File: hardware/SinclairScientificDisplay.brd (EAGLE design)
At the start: 47 x 17.8 mm, 6 parts

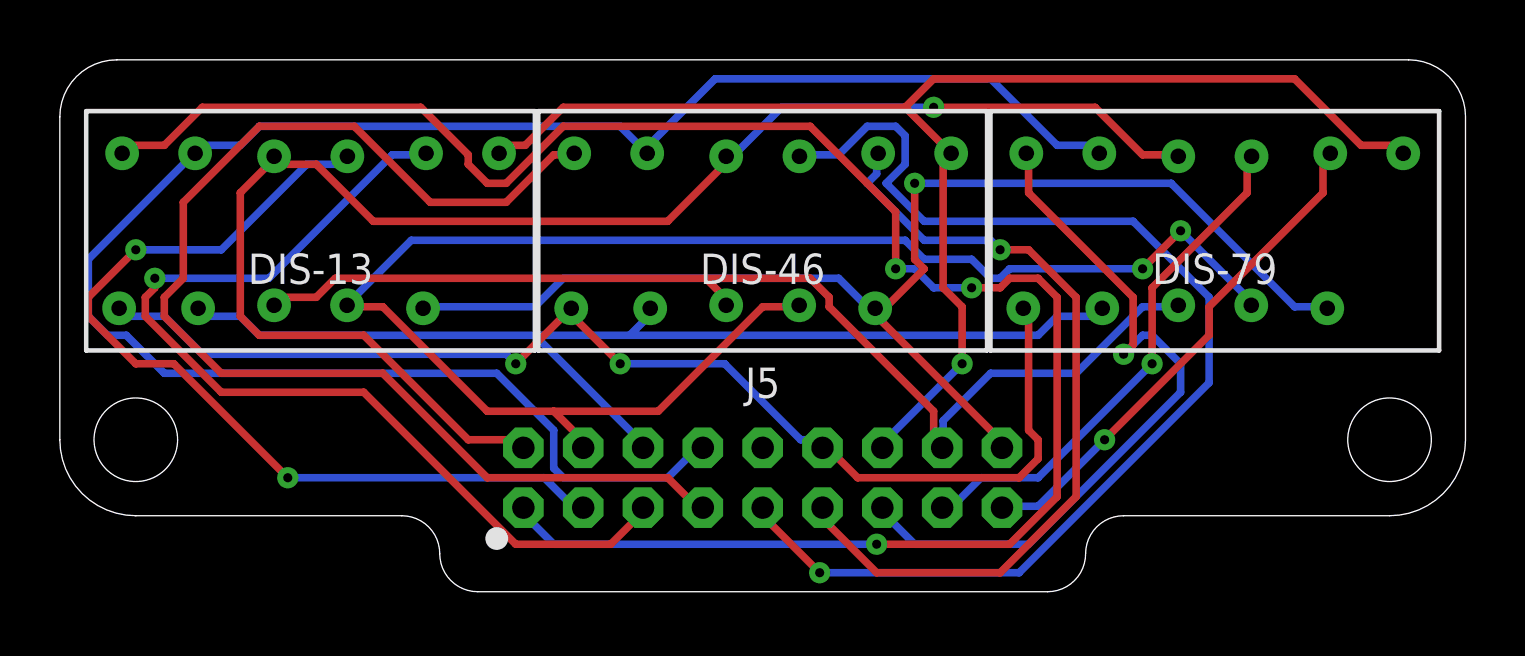
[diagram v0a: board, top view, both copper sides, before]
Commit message: Added some silkscreen labels and logo
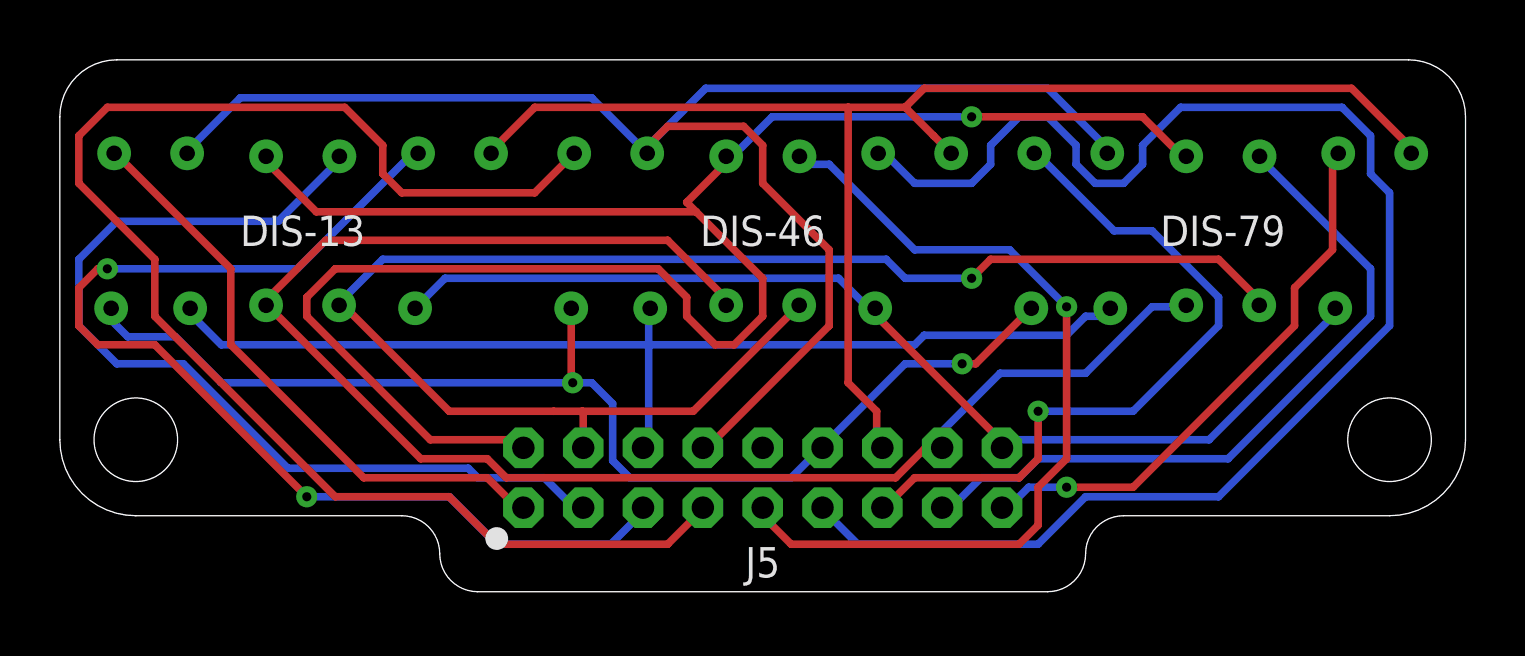
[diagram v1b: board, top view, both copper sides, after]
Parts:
- moved DIS-13 0.27 mm to (8.12, 12.1)
- moved DIS-79 0.27 mm to (38.9, 12.1)
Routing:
- net LED_CA1: track 63.5 -> 20.1 mm, vias 3 -> 0
- net LED_CA6: track 27.1 -> 50.4 mm, vias 1 -> 0
- net LED_DP: track 37.4 -> 53.4 mm
- net LED_F: track 50.6 -> 65.8 mm
- net LED_A: track 64.1 -> 51.8 mm
- net LED_CA5: track 39.8 -> 29.0 mm
- net LED_CA4: track 40.6 -> 48.3 mm
- net LED_G: track 43.3 -> 35.7 mm, vias 1 -> 0
- net LED_CA8: track 17.7 -> 24.2 mm, vias 1 -> 0
- net LED_CA3: track 32.5 -> 36.9 mm, vias 1 -> 2
- net LED_CA9: track 17.2 -> 18.7 mm
- net LED_CA2: track 30.9 -> 32.1 mm, vias 2 -> 0
- net LED_E: track 40.3 -> 39.3 mm
- net LED_D: track 37.4 -> 36.6 mm
- net LED_C: track 53.0 -> 52.2 mm, vias 2 -> 1
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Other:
- board text added: "1"
- board text added: "2"
- board text added: "3"
- board text added: "4"
- board text added: "5"
- board text added: "6"
- board text added: "7"
- board text added: "8"
- board text added: "9"
- board text added: "A"
- board text added: "B"
- board text added: "C"
- board text added: "D"
- board text added: "E"
- board text added: "F"
- board text added: "G"
- board text added: "P"

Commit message: Fixed some hardware issues found in testing v1B prototype
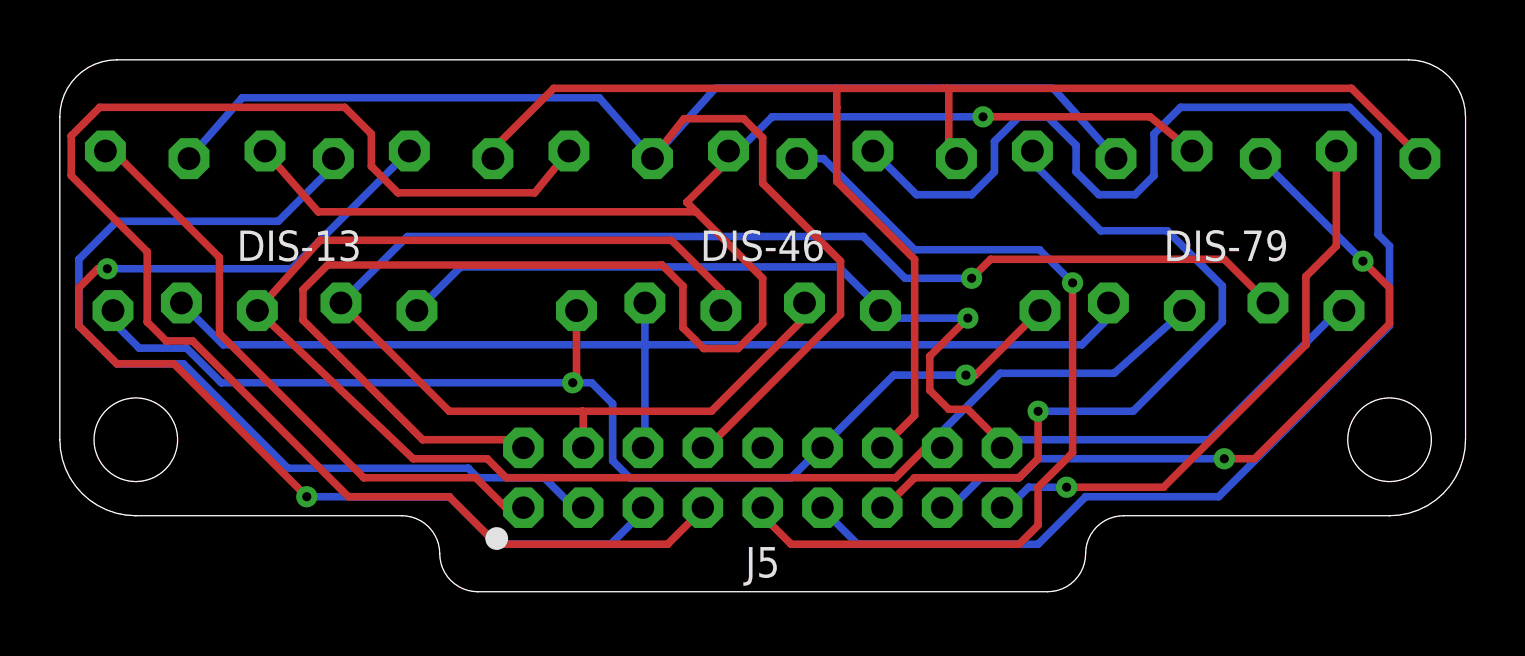
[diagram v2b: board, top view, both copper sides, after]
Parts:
- moved DIS-13 0.11 mm to (8.00, 12.1)
- moved DIS-79 0.11 mm to (39.0, 12.1)
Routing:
- net LED_G: track 35.7 -> 39.3 mm, vias 0 -> 1
- net LED_B: track 46.7 -> 49.2 mm
- net LED_CA6: track 50.4 -> 52.2 mm
- net LED_F: track 65.8 -> 67.4 mm
- net LED_C: track 52.2 -> 53.4 mm
- net LED_A: track 51.8 -> 53.0 mm
- net LED_CA8: track 24.2 -> 25.2 mm, vias 0 -> 2
- net LED_CA7: track 23.8 -> 24.5 mm
- net LED_D: track 36.6 -> 37.3 mm
- net LED_CA5: track 29.0 -> 29.7 mm
- net LED_CA4: track 48.3 -> 49.0 mm
- net LED_CA9: track 18.7 -> 19.3 mm
- net LED_DP: track 53.4 -> 54.0 mm

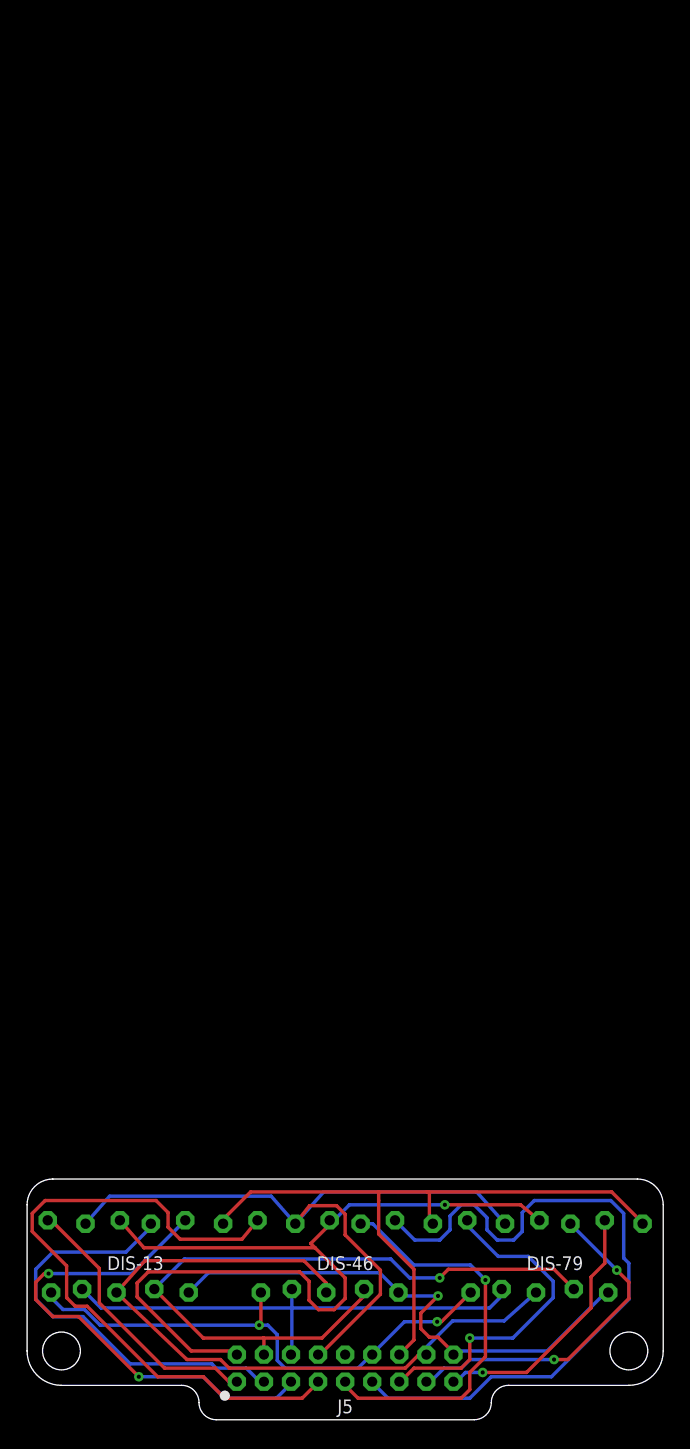
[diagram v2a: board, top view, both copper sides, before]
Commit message: Converted local library to managed library. Fixed more hardware issues found from testing v1B prototype.
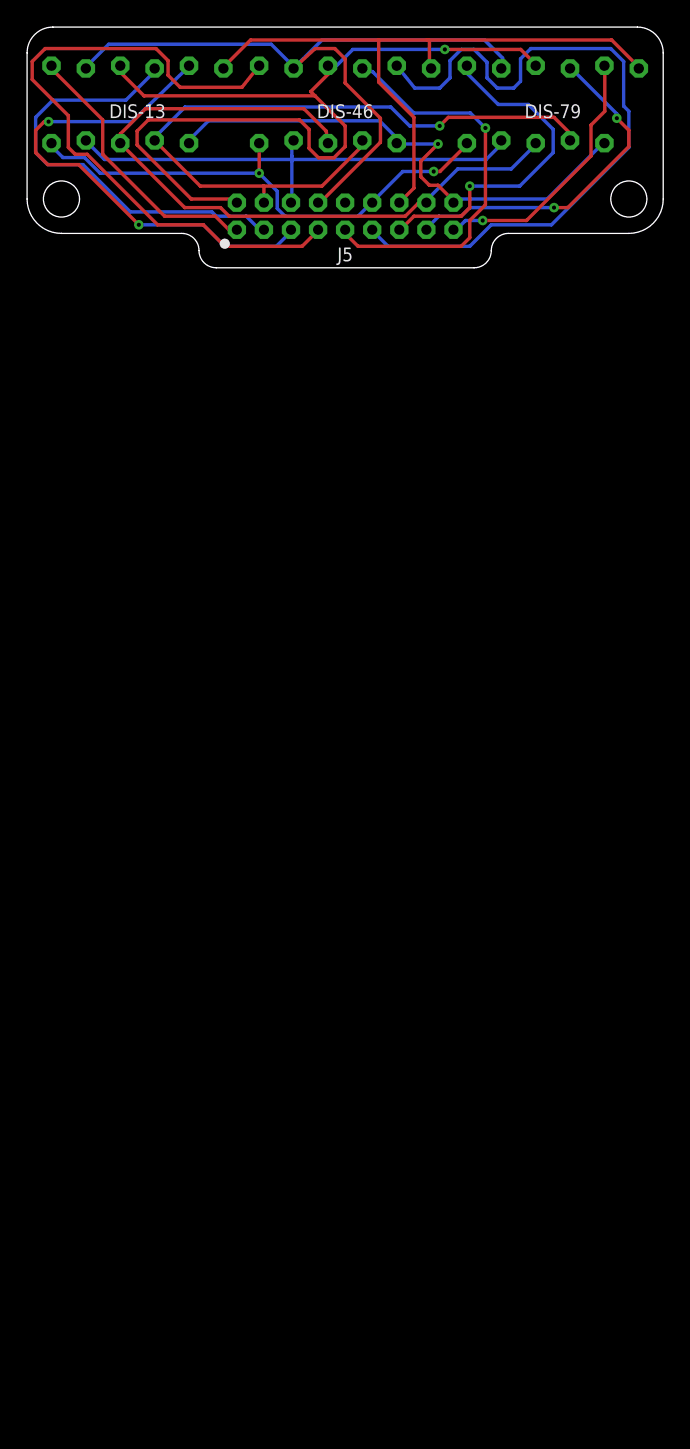
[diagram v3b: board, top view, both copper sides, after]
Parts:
- removed U$17, U$20: (no value), SinclairScientific:HOLE_3-48
- added U$1, U$2: (no value), SinclairScientific:HOLE_3-48
- moved DIS-13 85.1 mm to (8.15, 97.2)
- moved DIS-79 85.1 mm to (38.8, 97.2)
- moved DIS-46 85.1 mm to (23.5, 97.2)
- moved J5 85.1 mm to (23.5, 88.9)
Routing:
- net LED_E: track 39.6 -> 38.5 mm
- net LED_B: track 49.2 -> 48.5 mm
- net LED_CA6: track 52.2 -> 52.9 mm
- net LED_F: track 67.4 -> 68.1 mm
- net LED_CA2: track 32.0 -> 32.5 mm
- net LED_CA3: track 36.7 -> 37.2 mm
- net LED_CA7: track 24.5 -> 25.0 mm

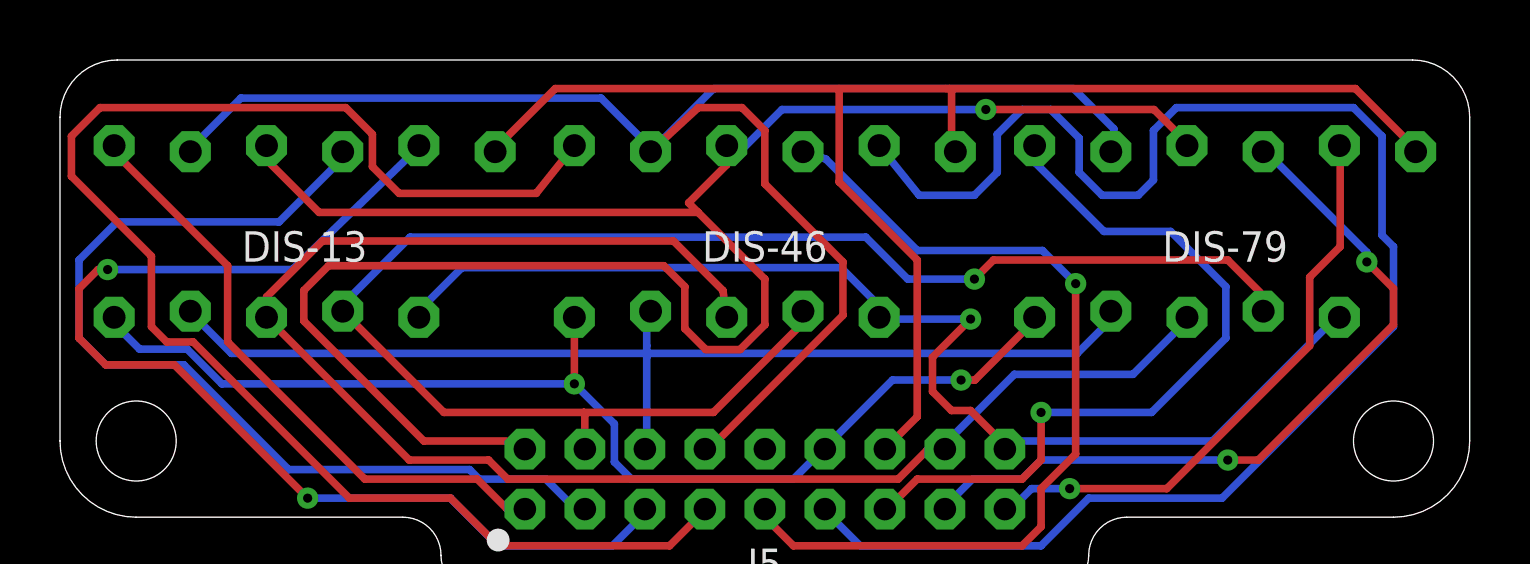
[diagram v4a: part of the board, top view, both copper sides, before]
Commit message: Changed button spacing, finalized rev 1C layouts
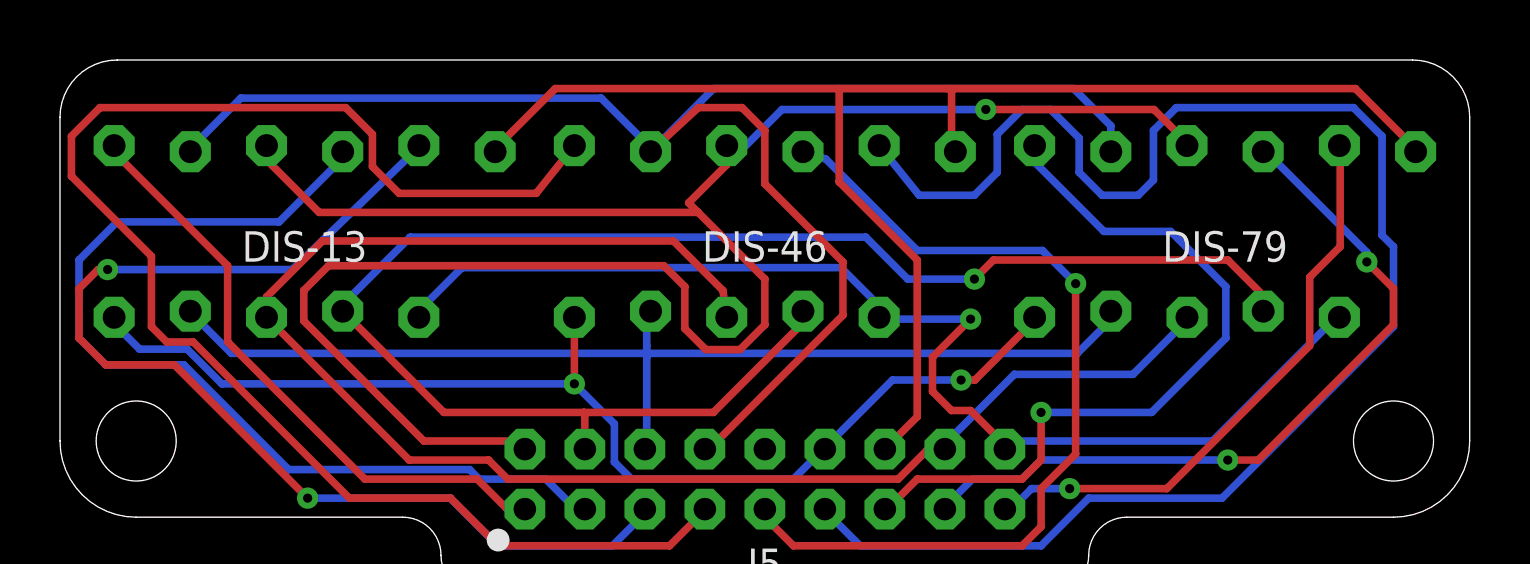
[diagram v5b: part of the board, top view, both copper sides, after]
